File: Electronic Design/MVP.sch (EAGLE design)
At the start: 36 parts, among them IC1 ACS712ELC-5A, IC3 ATMEGA328-PU, Q2 16MHz, Q3 IRF9540, Q4 IRF9540

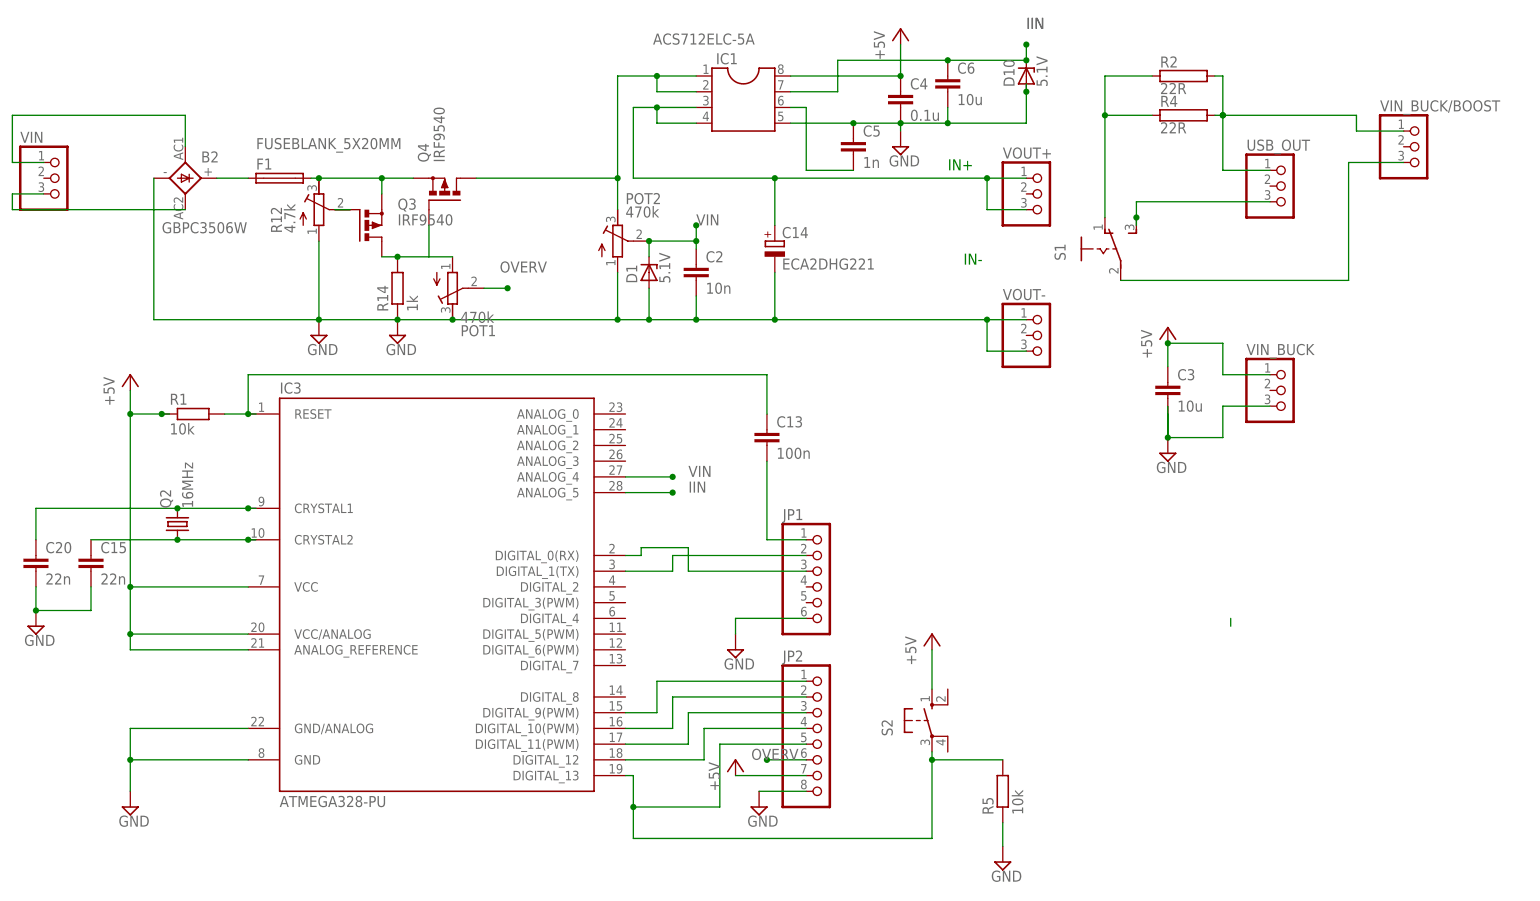
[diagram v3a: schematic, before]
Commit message: adding mounting holes
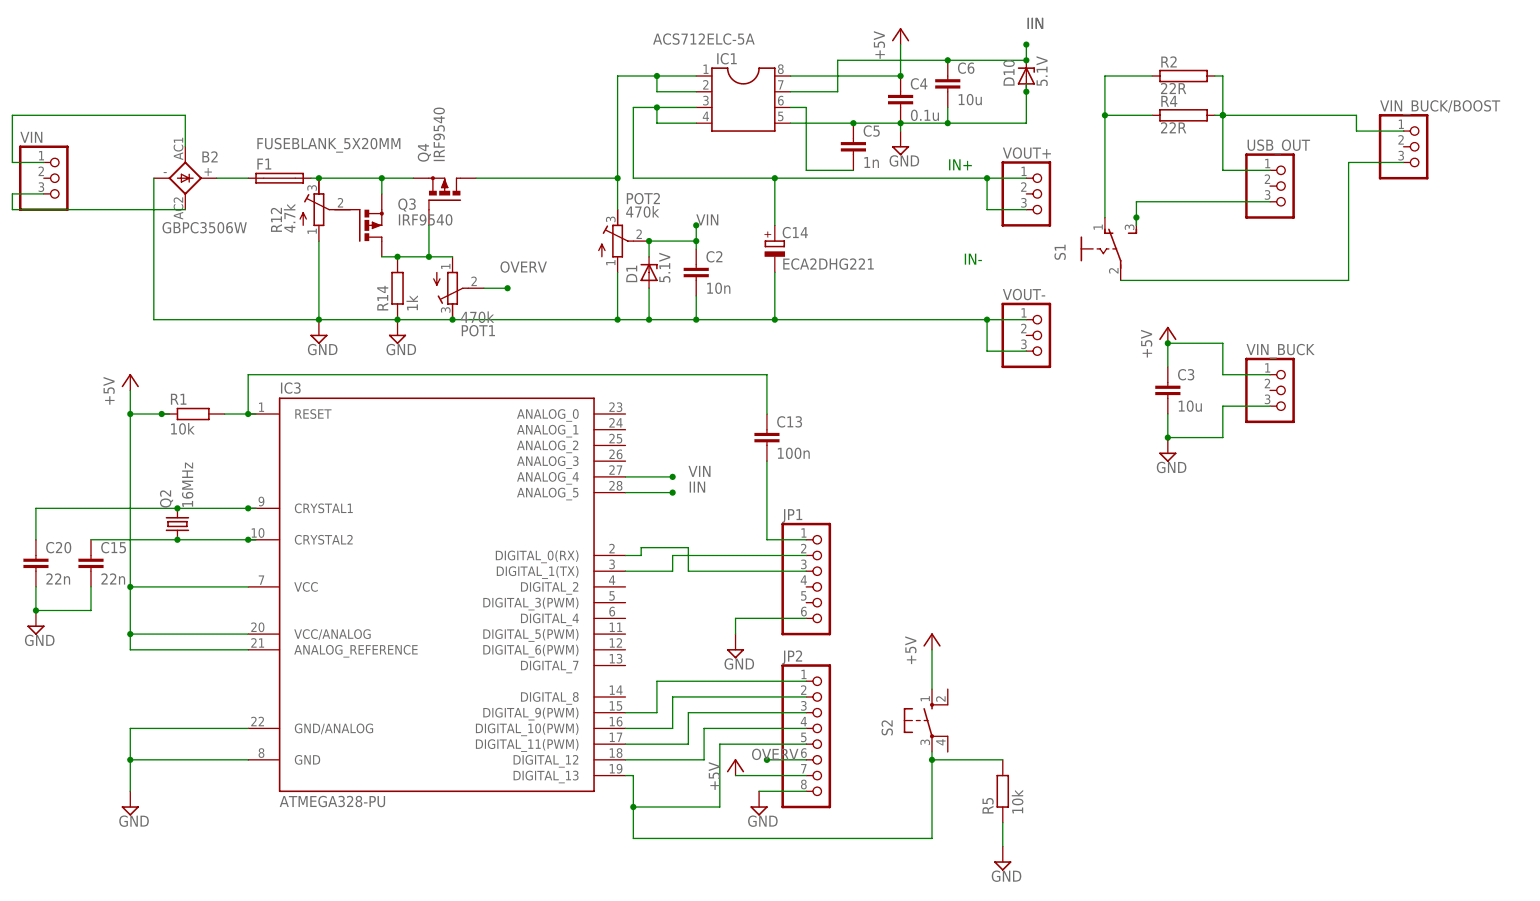
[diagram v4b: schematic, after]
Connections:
- removed net N$36: Q3.G, R12.S
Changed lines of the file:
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@@
 <setting verticaltext="up"/>
 </settings>
-<grid distance="0.1" unitdist="inch" unit="inch" style="lines" multiple="1" display="no" altdistance="0.01" altunitdist="inch" altunit="inch"/>
+<grid distance="0.05" unitdist="inch" unit="inch" style="lines" multiple="1" display="no" altdistance="0.01" altunitdist="inch" altunit="inch"/>
 <layers>
 <layer number="1" name="Top" color="4" fill="1" visible="no" active="no"/>
@@
 <segment>
 <pinref part="SUPPLY2" gate="GND" pin="GND"/>
-<wire x1="74.93" y1="52.07" x2="74.93" y2="46.99" width="0.1524" layer="91"/>
-<pinref part="C3" gate="G$1" pin="2"/>
-<junction x="74.93" y="46.99"/>
-<wire x1="74.93" y1="46.99" x2="74.93" y2="50.8" width="0.1524" layer="91"/>
 <wire x1="74.93" y1="46.99" x2="83.82" y2="46.99" width="0.1524" layer="91"/>
 <wire x1="83.82" y1="46.99" x2="83.82" y2="52.07" width="0.1524" layer="91"/>
 <pinref part="VIN_BUCK" gate="A" pin="3"/>
 <wire x1="83.82" y1="52.07" x2="91.44" y2="52.07" width="0.1524" layer="91"/>
+<pinref part="C3" gate="G$1" pin="2"/>
+<wire x1="74.93" y1="50.8" x2="74.93" y2="46.99" width="0.1524" layer="91"/>
+<junction x="74.93" y="46.99"/>
 </segment>
 <segment>
@@
 <pinref part="POT1" gate="G$1" pin="A"/>
 <wire x1="-40.64" y1="76.2" x2="-44.45" y2="76.2" width="0.1524" layer="91"/>
-</segment>
-</net>
-<net name="N$36" class="0">
-<segment>
-<pinref part="Q3" gate="G$1" pin="G"/>
-<pinref part="R12" gate="G$1" pin="S"/>
-<wire x1="-57.15" y1="83.82" x2="-59.69" y2="83.82" width="0.1524" layer="91"/>
+<junction x="-44.45" y="76.2"/>
 </segment>
 </net>
@@
 </segment>
 </net>
-<net name="N$7" class="0">
-<segment>
-<wire x1="85.09" y1="17.78" x2="85.09" y2="16.51" width="0.1524" layer="91"/>
-</segment>
-</net>

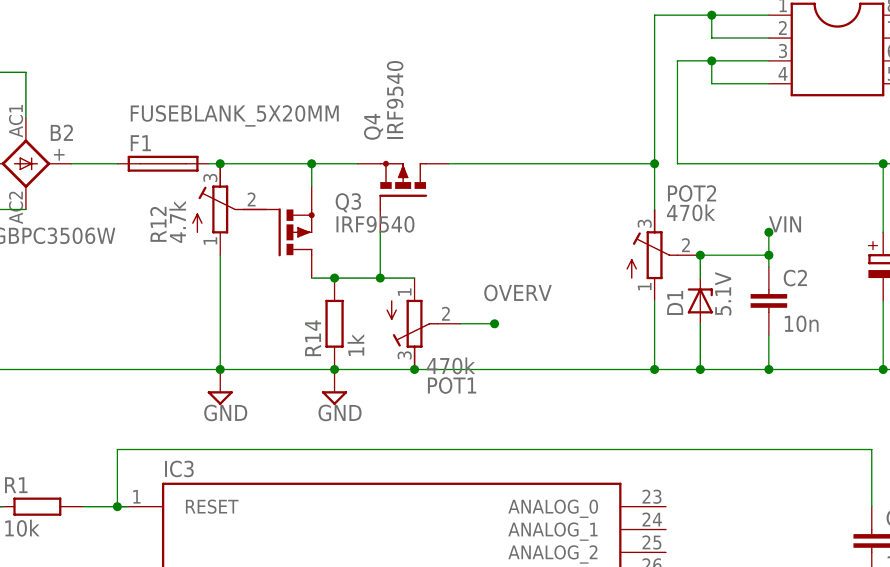
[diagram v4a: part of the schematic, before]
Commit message: making board more compact and replacing pots with 3296W as these are easier to find
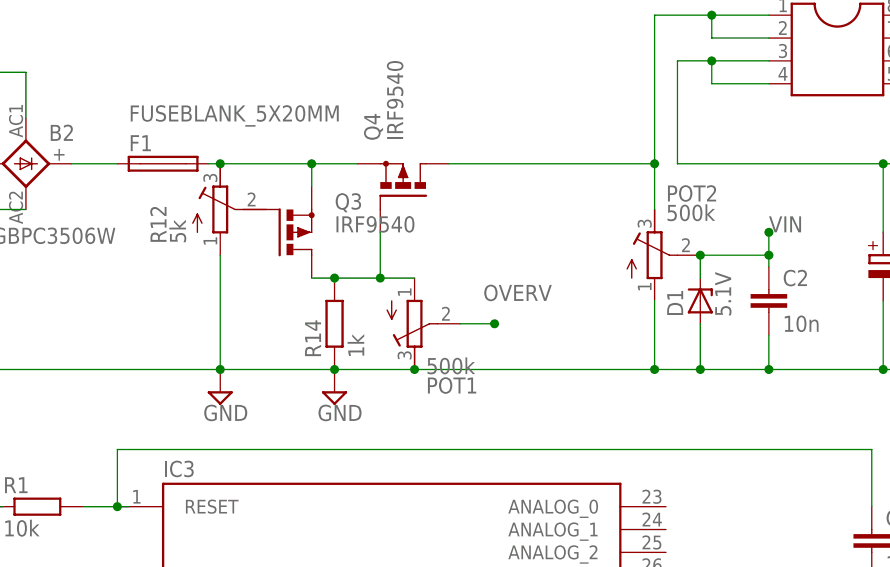
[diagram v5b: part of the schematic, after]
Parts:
- C14: device rcl:CPOL-EUE7.5-18 -> resistor:CPOL-EUE3.5-10
- POT1, POT2: value 470k -> 500k; device resistor:R-TRIMM4G/J -> resistor:R-TRIMM3296W
- R12: value 4.7k -> 5k; device resistor:R-TRIMM4G/J -> resistor:R-TRIMM3299W
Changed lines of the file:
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@@
 <setting verticaltext="up"/>
 </settings>
-<grid distance="0.05" unitdist="inch" unit="inch" style="lines" multiple="1" display="no" altdistance="0.01" altunitdist="inch" altunit="inch"/>
+<grid distance="0.1" unitdist="inch" unit="inch" style="lines" multiple="1" display="no" altdistance="0.01" altunitdist="inch" altunit="inch"/>
 <layers>
 <layer number="1" name="Top" color="4" fill="1" visible="no" active="no"/>
@@
 <part name="B2" library="rectifier" deviceset="GBPC6" device="" value="GBPC3506W"/>
 <part name="C2" library="resistor" deviceset="C-EU" device="C1210" value="10n"/>
-<part name="C14" library="rcl" deviceset="CPOL-EU" device="E7.5-18" value="ECA2DHG221"/>
+<part name="C14" library="resistor" deviceset="CPOL-EU" device="E3.5-10" value="ECA2DHG221"/>
 <part name="IC1" library="mylibrary" deviceset="SOIC8" device="" value="ACS712ELC-5A"/>
 <part name="C4" library="resistor" deviceset="C-EU" device="C1210" value="0.1u"/>
 <part name="SUPPLY1" library="supply2" deviceset="GND" device=""/>
-<part name="POT2" library="resistor" deviceset="R-TRIMM" device="4G/J" value="470k"/>
+<part name="POT2" library="resistor" deviceset="R-TRIMM" device="3296W" value="500k"/>
 <part name="D10" library="diode" deviceset="ZPD" device="" value="5.1V"/>
 <part name="Q3" library="transistor-power" deviceset="PMOSFET_P" device="TO220BV" value="IRF9540"/>
 <part name="Q4" library="transistor-power" deviceset="PMOSFET_P" device="TO220BV" value="IRF9540"/>
-<part name="R12" library="resistor" deviceset="R-TRIMM" device="4G/J" value="4.7k"/>
+<part name="R12" library="resistor" deviceset="R-TRIMM" device="3299W" value="5k"/>
 <part name="R14" library="resistor" deviceset="R-EU_" device="VTA52" value="1k"/>
 <part name="SUPPLY22" library="supply2" deviceset="GND" device=""/>
@@
 <part name="SUPPLY3" library="supply2" deviceset="GND" device=""/>
 <part name="+5V3" library="supply1" deviceset="+5V" device=""/>
-<part name="POT1" library="resistor" deviceset="R-TRIMM" device="4G/J" value="470k"/>
+<part name="POT1" library="resistor" deviceset="R-TRIMM" device="3296W" value="500k"/>
 <part name="D1" library="diode" deviceset="ZPD" device="" value="5.1V"/>
 <part name="C6" library="resistor" deviceset="C-EU" device="C1210" value="10u"/>

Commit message: changing component names so the make sense again
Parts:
- removed C14: ECA2DHG221, resistor:CPOL-EUE3.5-10
- removed Q4: IRF9540, transistor-power:PMOSFET_PTO220BV
- removed R14: 1k, resistor:R-EU_VTA52
- added C1: 10n, resistor:C-EUC1210
- added R3: 22R, resistor-power:RRWM8X45
- added X1: 16MHz, crystal:CRYSTALHC49S
- C2: value 10n -> ECA2DHG221; device resistor:C-EUC1210 -> resistor:CPOL-EUE3.5-10
- C3: value 10u -> 0.1u
- C4: value 0.1u -> 1n
- C5: value 1n -> 10u
- Q2: value 16MHz -> IRF9540; device crystal:CRYSTALHC49S -> transistor-power:PMOSFET_PTO220BV
- R1: value 10k -> 1k; device resistor:R-EU_R1210 -> resistor:R-EU_VTA52
- R4: value 22R -> 10k; device resistor-power:RRWM8X45 -> resistor:R-EU_R1206
- R5: device resistor:R-EU_R1210 -> resistor:R-EU_R1206
- renumbered B2 to B1, C13 to C7, C15 to C9, C20 to C8, D10 to D2, IC3 to IC2, Q3 to Q1, R12 to POT3
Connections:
- net +5V: now also C6.1, R4.1; no longer C4.1, R1.1
- net GND: now also C1.2, C2.-, C4.1, C5.2, R1.1; no longer C14.-, C2.2, C4.2, C5.1, R14.1
- net IIN: now also C5.1; no longer C6.1
- net M1S: now also C2.+; no longer C14.+
- net N$10: now also Q2.S; no longer Q4.S
- net N$15: now also X1.1; no longer Q2.1
- net N$16: now also X1.2; no longer Q2.2
- net N$17: now also R4.2; no longer R1.2
- net N$2: now also C4.2; no longer C5.2
- net N$23: now also R3.2; no longer R4.2
- net N$24: now also R3.1; no longer R4.1
- net N$3: now also Q2.D; no longer Q4.D
- net N$35: now also Q2.G, R1.2; no longer Q4.G, R14.2
- net VIN: now also C1.1; no longer C2.1
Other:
- moved on the sheet: C3, C4, C5, C6, R1

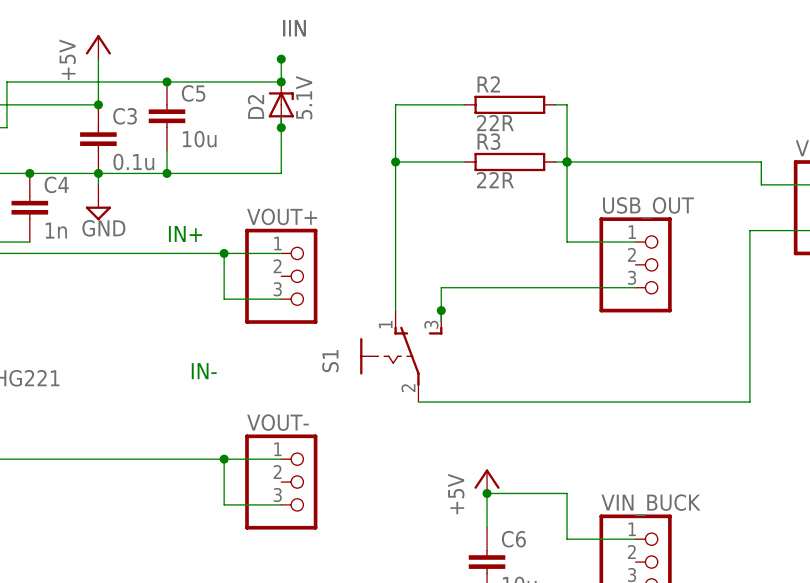
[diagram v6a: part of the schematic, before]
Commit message: replacing switch on PCB with pin header as originally intended
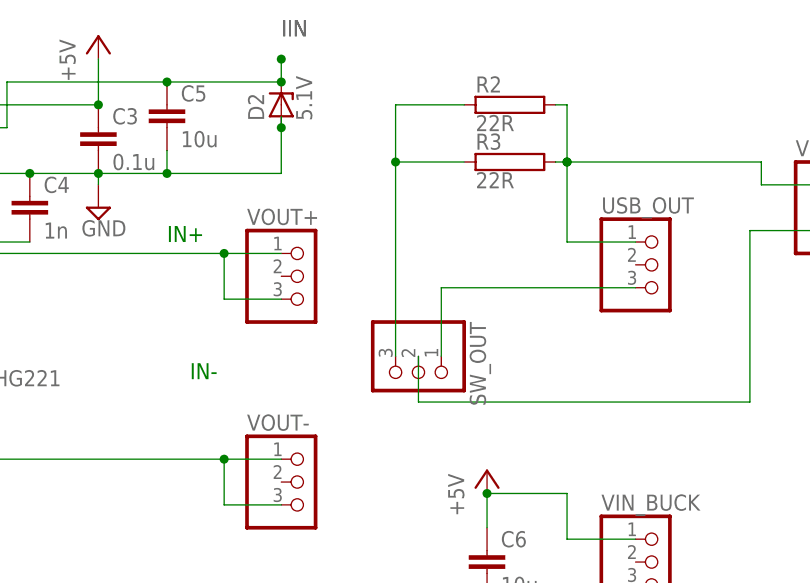
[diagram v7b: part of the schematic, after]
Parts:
- removed S1: (no value), switch:255SB
- added SW_OUT: (no value), pinhead:PINHD-1X3
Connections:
- net N$22: now also SW_OUT.2; no longer S1.P
- net N$24: now also SW_OUT.3; no longer S1.O
- net N$25: now also SW_OUT.1; no longer S1.S
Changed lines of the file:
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@@
 <setting verticaltext="up"/>
 </settings>
-<grid distance="0.1" unitdist="inch" unit="inch" style="lines" multiple="1" display="no" altdistance="0.01" altunitdist="inch" altunit="inch"/>
+<grid distance="0.05" unitdist="inch" unit="inch" style="lines" multiple="1" display="no" altdistance="0.01" altunitdist="inch" altunit="inch"/>
 <layers>
 <layer number="1" name="Top" color="4" fill="1" visible="no" active="no"/>
@@
 <part name="R2" library="resistor-power" deviceset="R" device="RWM8X45" value="22R"/>
 <part name="R3" library="resistor-power" deviceset="R" device="RWM8X45" value="22R"/>
-<part name="S1" library="switch" deviceset="255SB" device=""/>
 <part name="USB_OUT" library="pinhead" deviceset="PINHD-1X3" device=""/>
 <part name="S2" library="switch-omron" deviceset="10-XX" device=""/>
@@
 <part name="C5" library="resistor" deviceset="C-EU" device="C1210" value="10u"/>
 <part name="C4" library="resistor" deviceset="C-EU" device="C1210" value="1n"/>
+<part name="SW_OUT" library="pinhead" deviceset="PINHD-1X3" device=""/>
 </parts>
 <sheets>
@@
 <instance part="R2" gate="G$1" x="77.47" y="105.41"/>
 <instance part="R3" gate="G$1" x="77.47" y="99.06"/>
-<instance part="S1" gate="1" x="64.77" y="77.47"/>
 <instance part="USB_OUT" gate="A" x="93.98" y="87.63"/>
 <instance part="S2" gate="1" x="36.83" y="1.27"/>
@@
 <instance part="C5" gate="G$1" x="39.37" y="105.41"/>
 <instance part="C4" gate="G$1" x="24.13" y="95.25"/>
+<instance part="SW_OUT" gate="A" x="67.31" y="74.93" rot="R270"/>
 </instances>
 <busses>
@@
 <net name="N$22" class="0">
 <segment>
-<pinref part="S1" gate="1" pin="P"/>
 <wire x1="67.31" y1="72.39" x2="104.14" y2="72.39" width="0.1524" layer="91"/>
 <wire x1="104.14" y1="72.39" x2="104.14" y2="91.44" width="0.1524" layer="91"/>
 <pinref part="VIN_BUCK/BOOST" gate="A" pin="3"/>
 <wire x1="113.03" y1="91.44" x2="104.14" y2="91.44" width="0.1524" layer="91"/>
+<pinref part="SW_OUT" gate="A" pin="2"/>
+<wire x1="67.31" y1="72.39" x2="67.31" y2="77.47" width="0.1524" layer="91"/>
 </segment>
 </net>
@@
 <pinref part="R3" gate="G$1" pin="1"/>
 <wire x1="64.77" y1="99.06" x2="72.39" y2="99.06" width="0.1524" layer="91"/>
-<pinref part="S1" gate="1" pin="O"/>
-<wire x1="64.77" y1="99.06" x2="64.77" y2="82.55" width="0.1524" layer="91"/>
+<wire x1="64.77" y1="99.06" x2="64.77" y2="77.47" width="0.1524" layer="91"/>
 <junction x="64.77" y="99.06"/>
+<pinref part="SW_OUT" gate="A" pin="3"/>
 </segment>
 </net>
@@
 <pinref part="USB_OUT" gate="A" pin="3"/>
 <wire x1="91.44" y1="85.09" x2="69.85" y2="85.09" width="0.1524" layer="91"/>
-<wire x1="69.85" y1="85.09" x2="69.85" y2="82.55" width="0.1524" layer="91"/>
-<pinref part="S1" gate="1" pin="S"/>
-<wire x1="69.85" y1="82.55" x2="69.85" y2="81.28" width="0.1524" layer="91"/>
-<junction x="69.85" y="82.55"/>
-</segment>
-</net>
+<pinref part="SW_OUT" gate="A" pin="1"/>
+<wire x1="69.85" y1="85.09" x2="69.85" y2="77.47" width="0.1524" layer="91"/>
+</segment>
+</net>
